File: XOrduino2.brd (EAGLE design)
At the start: 81.3 x 53.5 mm, 77 parts, among them J1 2.5mm, J2 2.5mm, J3 2.5mm, J4 2.5mm, J5 Batt In, J6 MOT R, J7 MOT L, P1 10k, Q1 ALS-PT204-6C/L177, SW1 RESET, SW2 6mm Button, SW3 LEFT BUMPER, SW4 RIGHT BUMPER, U1 ATMEGA32U4-XUAU, U2 LMV358, U3 NJU7261, U4 DRV8833PWP, U5 QRE1113GR, U6 QRE1113GR, X1 USBPCB, X2 USBMINIB, X3 USBMICROB, Y1 16MHz

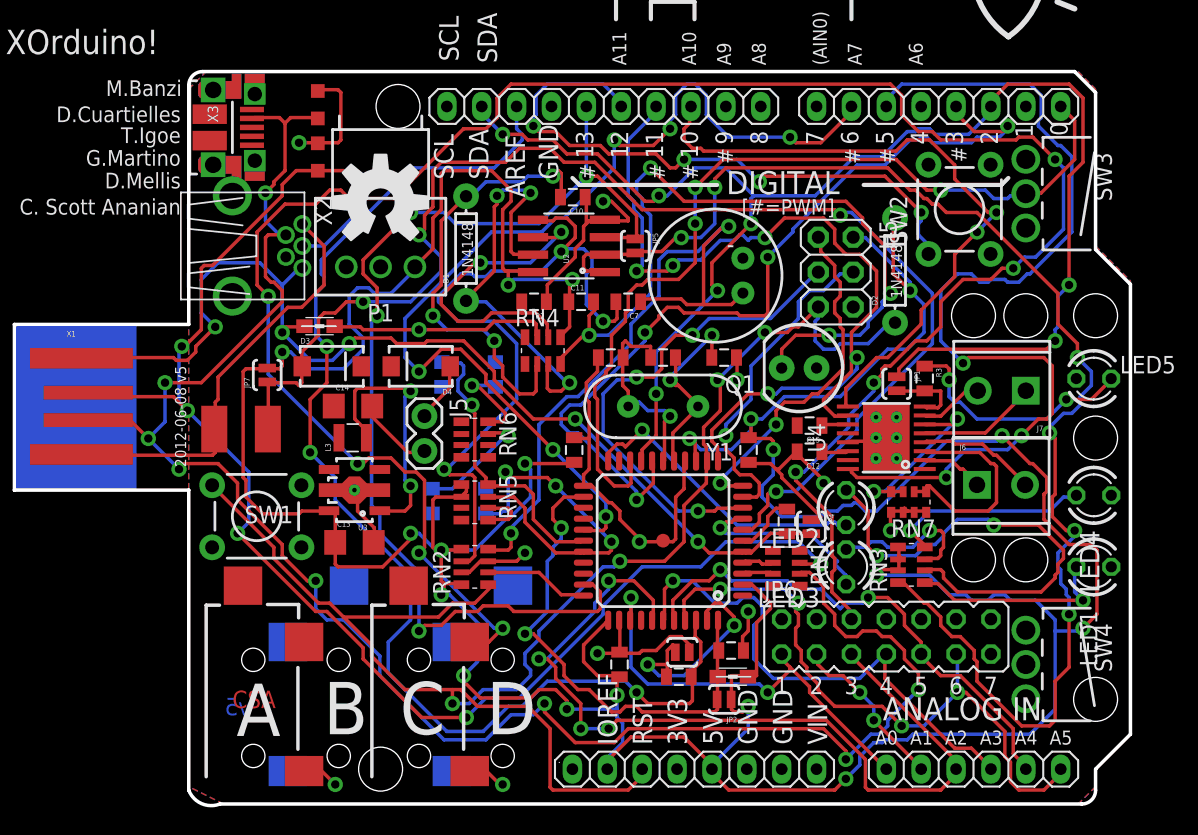
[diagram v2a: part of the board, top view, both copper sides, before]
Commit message: Almost-completely 4-layer routed version of XOrduino2.
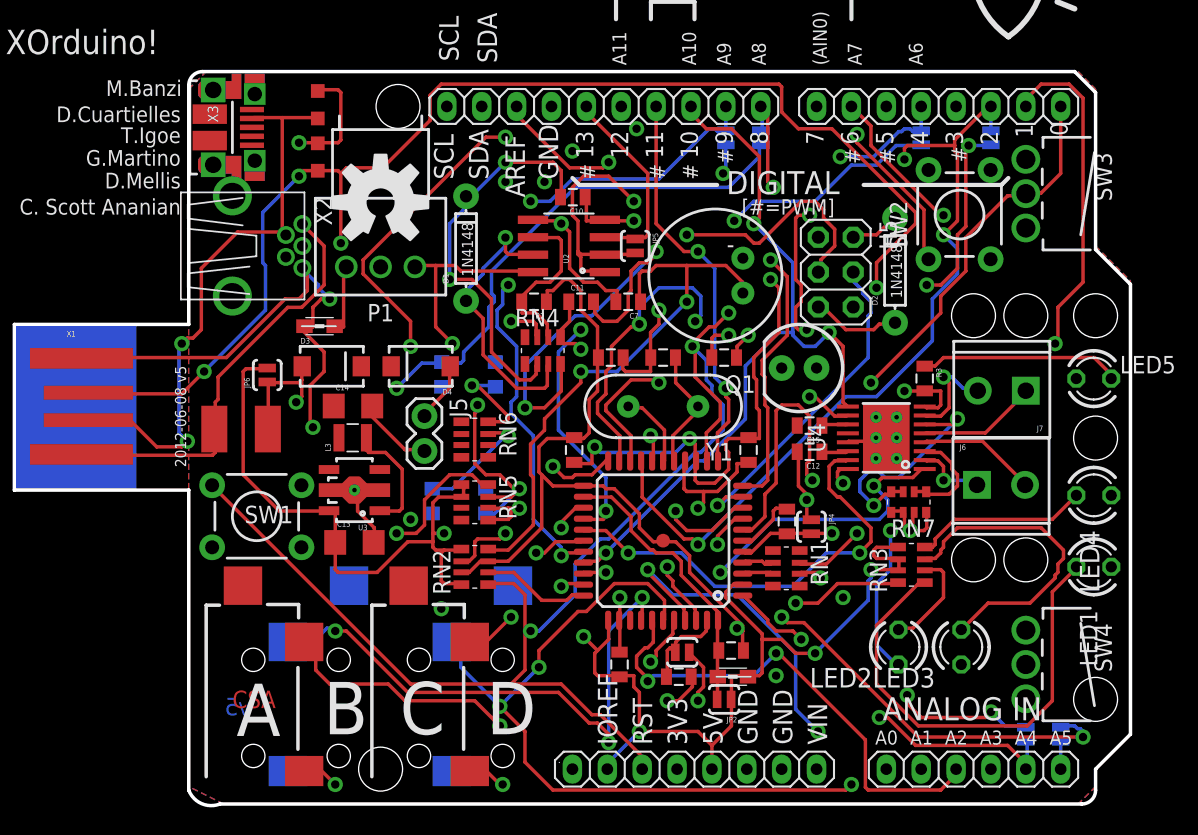
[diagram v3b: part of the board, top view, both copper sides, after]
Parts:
- added JP10, JP11, JP8, JP9: N/C, xorduino:SJ-2S-BOT-TRACE-NOCONFLICT
- JP1, JP7: device xorduino:SJ-2S-TRACE-NOCONFLICT -> xorduino:SJ-2S-BOT-TRACE-NOCONFLICT
- JP6: value Sensor Routing -> N/C; device xorduino:JP7QS-NOCONFLICT -> xorduino:SJ-2S-TRACE-NOCONFLICT
- moved JP7 61.1 mm to (73.7, 5.08)
- moved JP6 48.9 mm to (18.4, 31.2), turned to 90 degrees
- moved JP1 19.2 mm to (71.1, 48.5)
- moved LED2 10.9 mm to (64.4, 11.4)
- moved LED3 10.2 mm to (69.0, 11.4)
- moved SW2 0.38 mm to (68.8, 42.9)
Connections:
- net D+ renamed D_P
- net D- renamed D_M
- net RD+ renamed RD_P
- net RD- renamed RD_M
- removed net RA: J1.2, JP6.2
- removed net RB: J2.2, JP6.4
- removed net RC: J3.2, JP6.6
- removed net RD: J4.2, JP6.8
- new net N$21: JP10.1, RN5.8, U5.3
- new net N$22: JP11.1, RN5.7, U6.3
- net +5V: now also JP6.2; no longer JP7.2
- net A0: now also J1.2; no longer JP6.1
- net A1: now also J2.2; no longer JP6.3
- net A2: now also J3.2; no longer JP6.5
- net A3: now also J4.2; no longer JP6.7
- net A4: now also JP7.1; no longer JP6.9
- net A5: now also JP8.1; no longer JP6.11
- net D4: now also JP9.1; no longer JP6.13
- net IO8: now also JP10.2; no longer RN5.8, U5.3
- net IO9*: now also JP11.2; no longer RN5.7, U6.3
- net LIGHT: now also JP8.2; no longer JP6.12
- net SLIDER: now also JP9.2; no longer JP6.14
- net SOUND: now also JP7.2; no longer JP6.10
- net VUSB: now also JP6.1; no longer JP7.1
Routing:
- net RC: track 156.3 -> 0.00 mm, vias 8 -> 0
- net +5V: track 319.4 -> 213.5 mm, vias 19 -> 10
- net D1/TX: track 0.00 -> 96.9 mm, vias 0 -> 3
- net D4: track 0.00 -> 82.0 mm, vias 0 -> 5
- net SOUND: track 32.4 -> 102.1 mm, vias 3 -> 5
- net N$21: track 0.00 -> 57.6 mm, vias 0 -> 2
- net A1: track 12.1 -> 64.5 mm, vias 2 -> 3
- net N$22: track 0.00 -> 50.0 mm, vias 0 -> 4
- net D7: track 0.00 -> 49.1 mm, vias 0 -> 1
- net SLIDER: track 0.00 -> 43.4 mm, vias 0 -> 1
- net N$8: track 3.94 -> 44.9 mm, vias 0 -> 3
- net LIGHT: track 56.5 -> 96.8 mm
- net IO8: track 21.2 -> 60.1 mm, vias 1 -> 3
- net D_M: track 132.4 -> 95.3 mm, vias 8 -> 3
- net AREF: track 88.4 -> 57.9 mm
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
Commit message: 97% routed 4-layer XOrduino.
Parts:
- added JP12: SERVO, SparkFun-Connectors:1X03
- JP1, JP7, JP8, JP9: device xorduino:SJ-2S-BOT-TRACE-NOCONFLICT -> xorduino:SJ-2S-BOT-TRACE-VIA-NOCONFLICT
- X3: value USBMICROB -> USBMICROB-VIA; device xorduino:USB-MICROB -> xorduino:USB-MICROB-VIA
- moved J5 34.1 mm to (58.4, 9.53), turned to 180 degrees
- moved JP7 0.51 mm to (73.7, 4.57), turned to 270 degrees
- moved JP8 0.51 mm to (76.2, 4.57), turned to 270 degrees
- moved JP9 0.25 mm to (66.0, 48.8), turned to 90 degrees
- moved JP1 0.13 mm to (71.1, 48.6), turned to 90 degrees
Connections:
- removed net N$17: D4.A, J5.1
- new net VCCIO: C14.1, C15.2, D3.C, D4.C, JP12.2, L3.1, LED5.A, RN5.3, RN5.4, RN6.1, RN6.2, U3.4, U4.12
- net A4: now also JP7.2; no longer JP7.1
- net A5: now also JP8.2; no longer JP8.1
- net D2/SDA: now also JP1.2; no longer JP1.1
- net D4: now also JP9.2; no longer JP9.1
- net D7: now also JP10.2
- net D_M: now also X3.D-_VIA
- net D_P: now also X3.D+_VIA
- net GND: now also JP12.1
- net IO8: now also JP11.2; no longer JP10.2
- net IO9*: now also JP12.3; no longer JP11.2
- net LIGHT: now also JP8.1, JP8.VIA6; no longer JP8.2
- net N$12: now also JP1.1, JP1.VIA6; no longer JP1.2
- net SLIDER: now also JP9.1, JP9.VIA6; no longer JP9.2
- net SOUND: now also JP7.1, JP7.VIA6; no longer JP7.2
- net UGND: now also X3.GND_VIA
- net VIN: now also D4.A, J5.1; no longer C14.1, C15.2, D3.C, D4.C, L3.1, LED5.A, RN5.3, RN5.4, RN6.1, RN6.2, U3.4, U4.12
- net XUSB: now also X3.VBUS_VIA
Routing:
- net GND: track 130.0 -> 443.4 mm, vias 12 -> 18
- net VCCIO: track 0.00 -> 203.8 mm, vias 0 -> 8
- net D_M: track 95.3 -> 186.4 mm, vias 3 -> 11
- net D_P: track 118.6 -> 205.1 mm, vias 5 -> 13
- net D5*: track 61.1 -> 135.4 mm, vias 3 -> 10
- net VIN: track 0.00 -> 67.7 mm, vias 0 -> 3
- net D4: track 82.0 -> 20.1 mm, vias 5 -> 3
- net +5V: track 213.5 -> 275.1 mm, vias 10 -> 16
- net D2/SDA: track 91.0 -> 138.4 mm, vias 4 -> 6
- net UGND: track 84.6 -> 131.3 mm, vias 3 -> 7
- net N$8: track 44.9 -> 91.1 mm, vias 3 -> 5
- net IO9*: track 49.1 -> 94.0 mm, vias 3 -> 5
- net A5: track 45.4 -> 1.98 mm, vias 2 -> 0
- net A4: track 36.6 -> 3.76 mm, vias 2 -> 0
- net MISO: track 23.6 -> 54.9 mm, vias 1 -> 4
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- added copper zone on layer 15, net +5V
- added copper zone on layer 2, net GND
- added copper zone on layer 1, net VCCIO
- removed copper zone on layer 1, net VIN

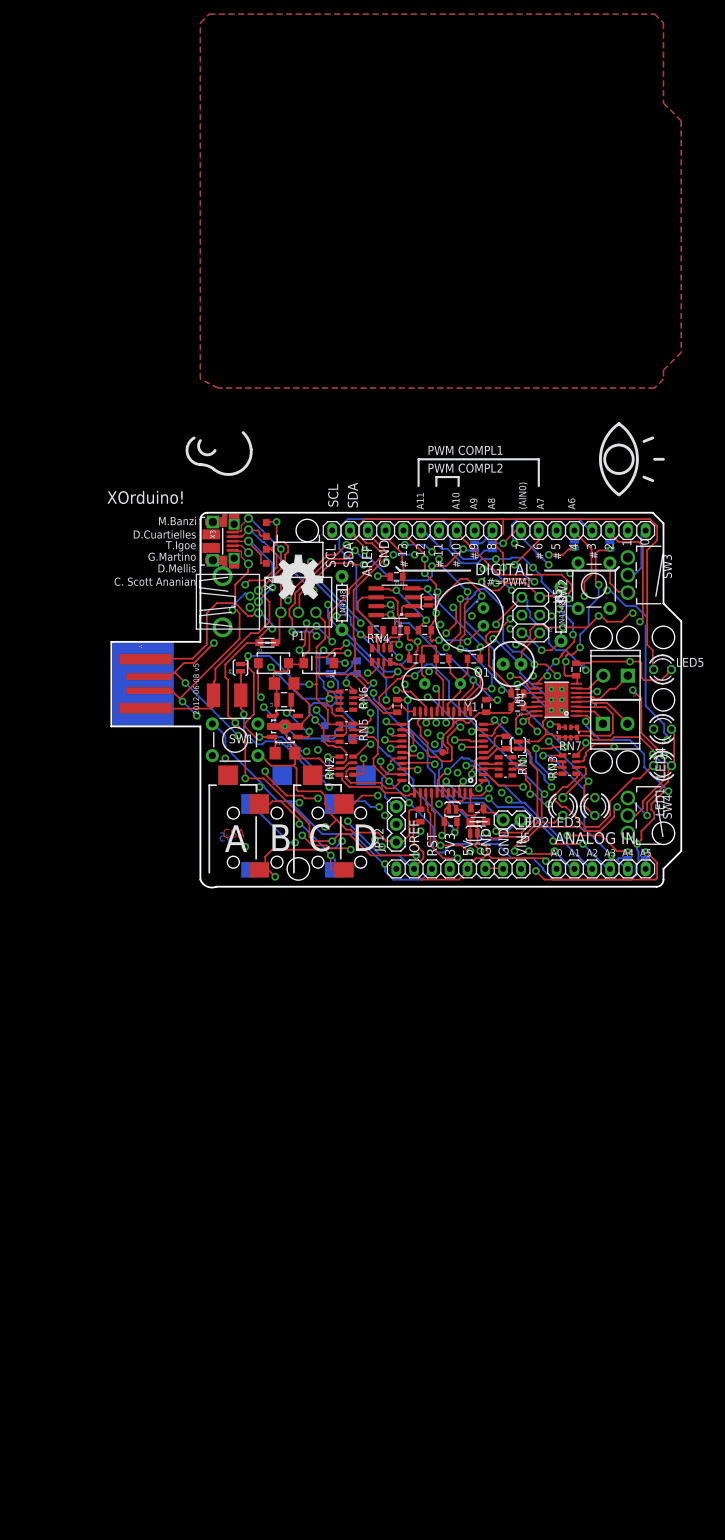
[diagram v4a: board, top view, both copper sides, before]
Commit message: First fully-routed version of XOrduino2 (4-layer).
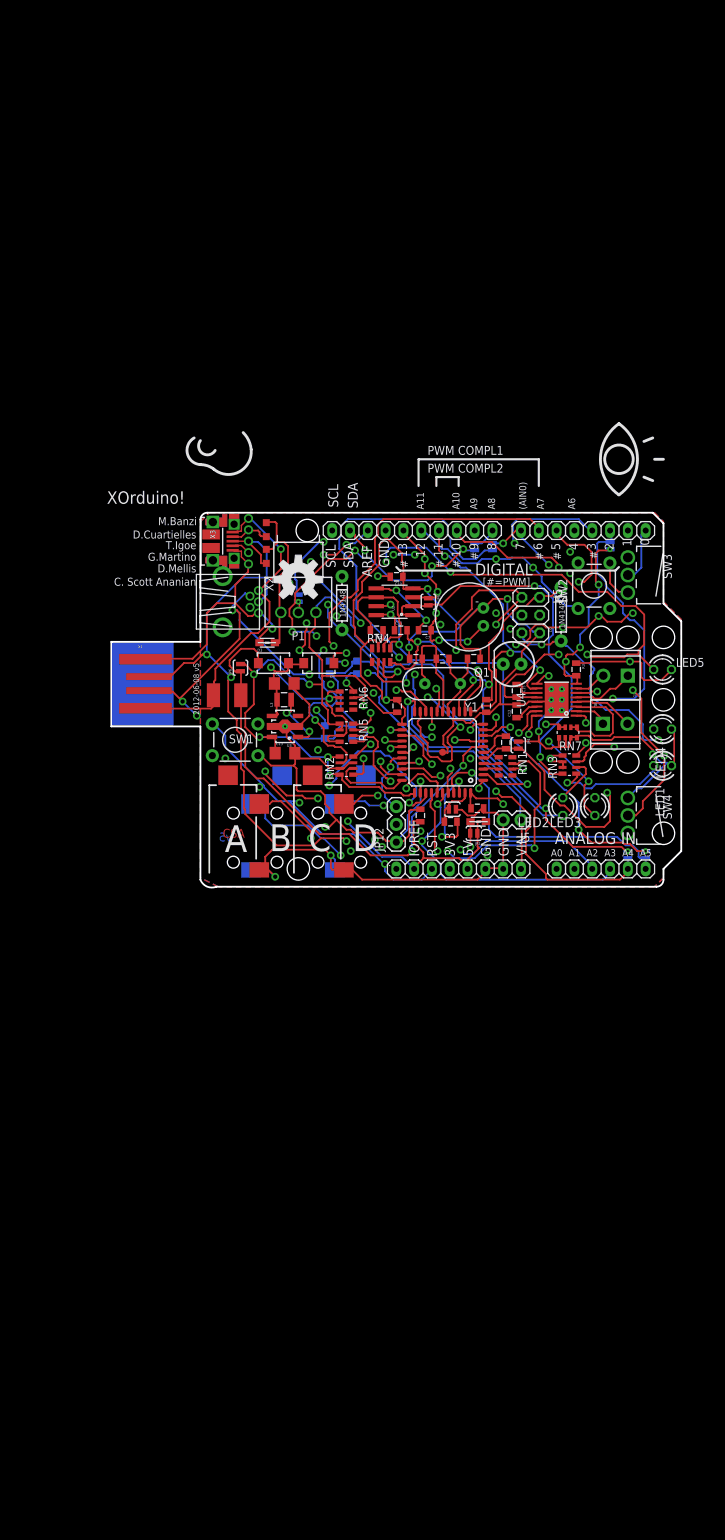
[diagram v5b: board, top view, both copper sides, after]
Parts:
- moved JP9 40.1 mm to (26.7, 41.1)
- moved C12 0.65 mm to (57.8, 25.0), turned to 90 degrees
- moved C15 0.40 mm to (57.8, 27.9), turned to 270 degrees
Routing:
- net D_M: track 186.4 -> 105.6 mm, vias 11 -> 5
- net D4: track 20.1 -> 97.8 mm, vias 3 -> 4
- net D_P: track 205.1 -> 131.3 mm, vias 13 -> 5
- net D5*: track 135.4 -> 79.4 mm, vias 10 -> 4
- net SLIDER: track 50.5 -> 1.76 mm, vias 2 -> 0
- net A4: track 3.76 -> 43.4 mm, vias 0 -> 2
- net N$8: track 91.1 -> 51.8 mm, vias 5 -> 2
- net A5: track 1.98 -> 41.1 mm, vias 0 -> 1
- net SOUND: track 120.2 -> 87.7 mm, vias 7 -> 4
- net UGND: track 131.3 -> 157.7 mm, vias 7 -> 3
- net LIGHT: track 89.4 -> 63.4 mm, vias 3 -> 2
- net D2/SDA: track 138.4 -> 113.3 mm, vias 6 -> 4
- net TXLED: track 58.4 -> 33.5 mm, vias 3 -> 1
- net +5V: track 275.1 -> 250.3 mm, vias 16 -> 12
- net A0: track 60.9 -> 83.6 mm, vias 3 -> 4
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
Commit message: Tweaks for better 2-layer routability.
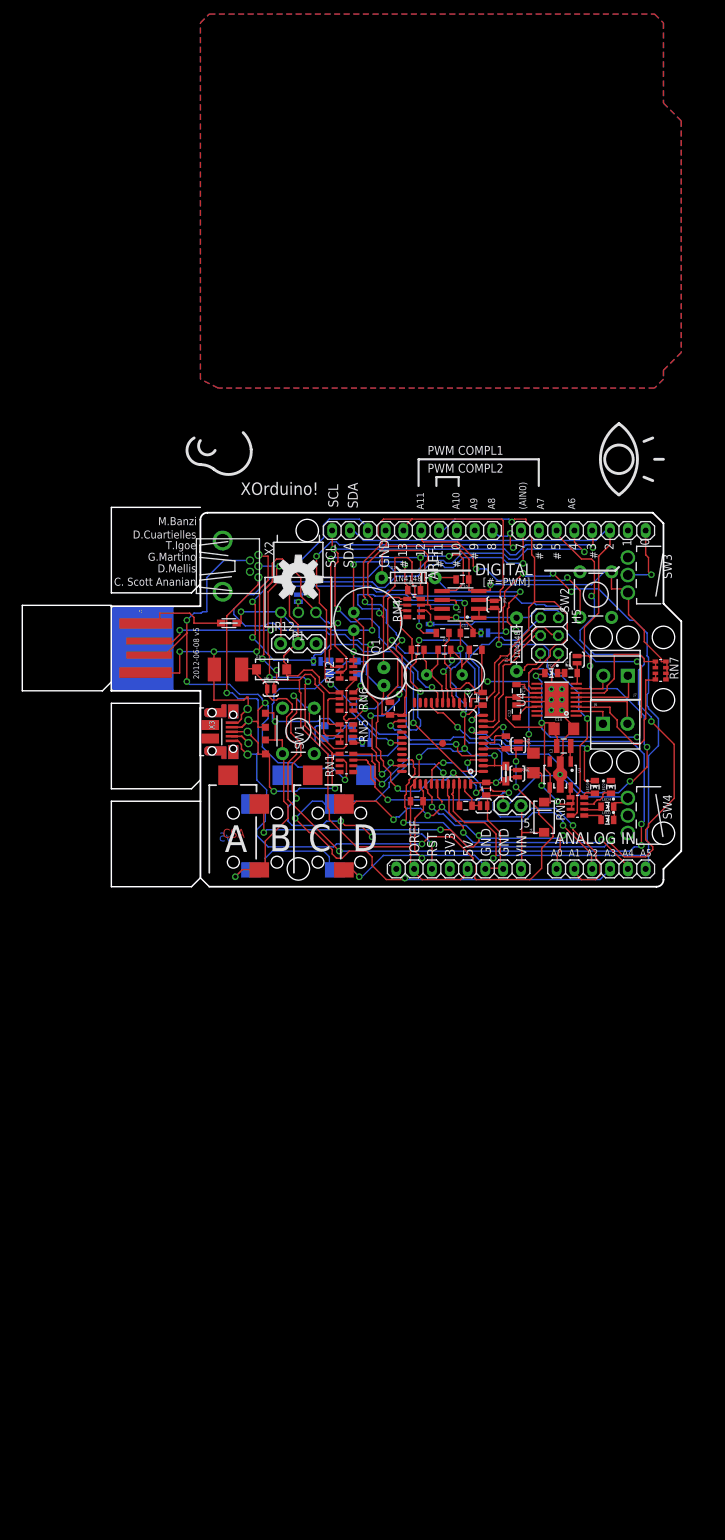
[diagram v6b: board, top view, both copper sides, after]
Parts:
- JP1: device xorduino:SJ-2S-BOT-TRACE-VIA-NOCONFLICT -> xorduino:SJ-2S-TRACE-NOCONFLICT
- JP10, JP11: device xorduino:SJ-2S-BOT-TRACE-NOCONFLICT -> xorduino:SJ-2S-BOT-TRACE-VIA-NOCONFLICT
- LED1, LED2, LED3, LED4, LED5: device led:LED3MM -> xorduino:LED0805
- moved JP7 42.9 mm to (45.5, 37.0)
- moved L3 40.4 mm to (64.5, 20.1)
- moved C14 40.4 mm to (64.5, 22.5)
- moved U3 39.8 mm to (64.0, 16.0), turned to 180 degrees
- moved JP8 39.1 mm to (53.2, 36.2), turned to 0 degrees
- moved D4 38.9 mm to (61.7, 9.91), turned to 90 degrees
- moved C13 35.5 mm to (60.2, 17.7), turned to 90 degrees
- moved JP12 32.8 mm to (24.1, 34.7), turned to 0 degrees
- moved JP11 31.9 mm to (36.3, 20.6), turned to 0 degrees
- moved JP10 29.9 mm to (29.3, 32.1), turned to 0 degrees
- moved X3 27.2 mm to (14.4, 22.1)
- moved Z2 27.2 mm to (22.0, 23.7)
- moved Z1 27.2 mm to (22.0, 19.9)
- moved RN1 22.7 mm to (33.5, 17.7), turned to 90 degrees
- moved Q1 18.4 mm to (38.9, 30.0), turned to 90 degrees
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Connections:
- new net PAD: U1.P$1
- net +5V: now also RN2.7, RN5.3, RN5.4; no longer RN2.5, RN5.1, RN5.2
- net D7: now also JP10.1, JP10.VIA6; no longer JP10.2
- net D_P: now also RN1.5; no longer RN1.7
- net GND: now also LED1.C, LED4.C, RN2.4; no longer LED1.K, LED4.K, RN2.7, U1.P$1
- net HWB: now also RN2.5; no longer RN2.2
- net N$1: now also RN3.4; no longer RN3.3
- net N$12: no longer JP1.VIA6
- net N$18: now also LED5.C; no longer LED5.K
- net N$19: now also RN7.1, RN7.2; no longer RN7.3, RN7.4
- net N$20: now also RN7.3, RN7.4; no longer RN7.1, RN7.2
- net N$21: now also JP10.2, RN5.6; no longer JP10.1, RN5.8
- net N$22: now also JP11.VIA6, RN5.5; no longer RN5.7
- net N$3: now also RN3.2; no longer RN3.4
- net N$4: now also RN3.3; no longer RN3.2
- net N$8: now also RN5.7, RN5.8; no longer RN5.5, RN5.6
- net N$9: now also RN2.2; no longer RN2.4
- net RD_P: now also RN1.4; no longer RN1.2
- net RXLED: now also LED3.C; no longer LED3.K
- net TXLED: now also LED2.C; no longer LED2.K
- net VCCIO: now also RN5.1, RN5.2; no longer RN5.3, RN5.4
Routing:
- net D1/TX: track 108.9 -> 0.00 mm, vias 8 -> 0
- net IO9*: track 94.0 -> 0.00 mm, vias 5 -> 0
- net D6*: track 92.6 -> 0.00 mm, vias 3 -> 0
- net IO10*: track 72.7 -> 0.00 mm, vias 3 -> 0
- net N$21: track 71.7 -> 1.34 mm, vias 3 -> 0
- net A5: track 41.1 -> 107.1 mm, vias 1 -> 5
- net N$22: track 65.7 -> 3.36 mm, vias 7 -> 0
- net VIN: track 68.4 -> 12.3 mm, vias 3 -> 0
- net GND: track 436.8 -> 385.8 mm
- net N$8: track 51.8 -> 0.91 mm, vias 2 -> 0
- net SOUND: track 87.7 -> 39.0 mm, vias 4 -> 2
- net D_P: track 131.3 -> 83.0 mm, vias 5 -> 7
- net IO12: track 79.9 -> 32.0 mm, vias 5 -> 2
- net D7: track 53.4 -> 100.4 mm, vias 3 -> 4
- net D0/RX: track 56.7 -> 10.0 mm, vias 3 -> 1
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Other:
- board size 81.3 x 53.5 mm -> 94 x 54.1 mm
